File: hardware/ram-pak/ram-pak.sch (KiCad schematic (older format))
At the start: 16 parts, among them J1 PinHeader_2x22_P1.27mm, U1 TLV62568DBV

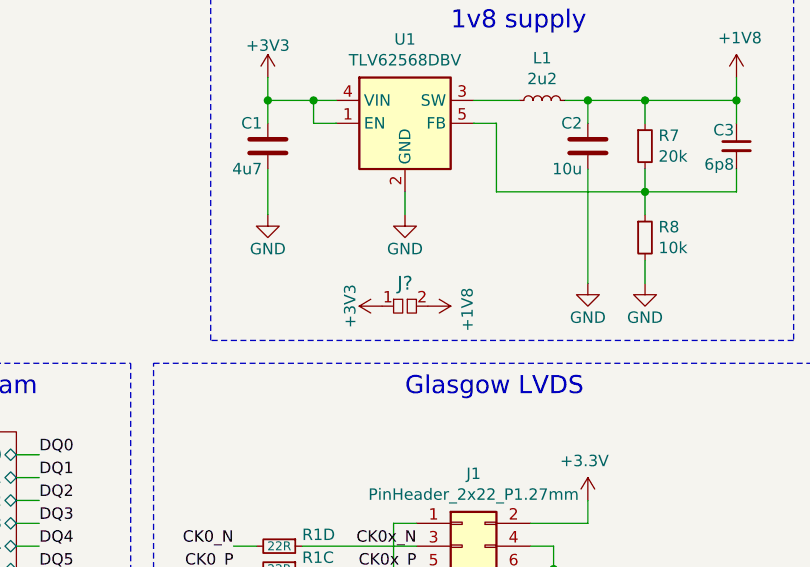
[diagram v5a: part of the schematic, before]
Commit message: ram-pak: Increased pad hole gap for improved assembly.
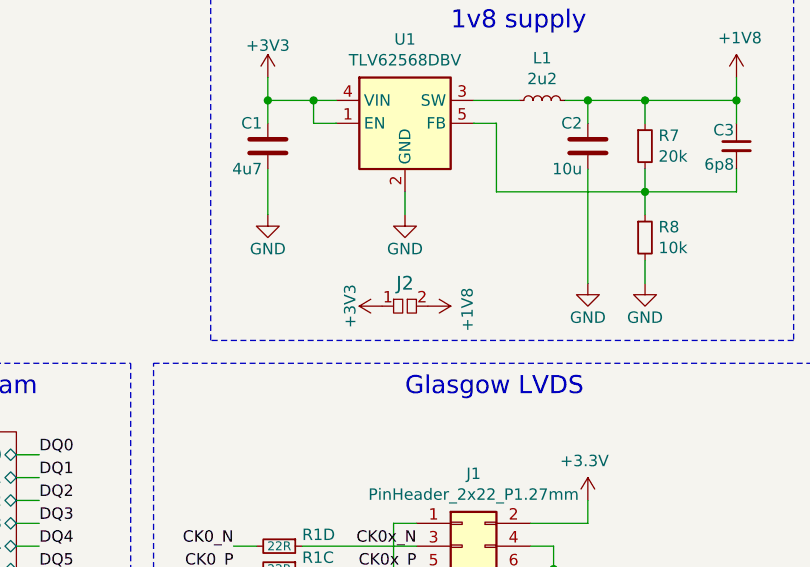
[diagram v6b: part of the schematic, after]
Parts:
- gave numbers to parts that had none: 1
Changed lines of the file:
@@
 DQ5x
 $Comp
-L pkl_misc:pkl_jumper J?
+L pkl_misc:pkl_jumper J2
 U 1 1 602E83F4
 P 6050 2500
-F 0 "J?" H 6050 2600 60  0000 C CNN
+F 0 "J2" H 6050 2600 60  0000 C CNN
 F 1 "pkl_jumper" H 6050 2641 60  0001 C CNN
 F 2 "pkl_jumpers:J_0603" H 6050 2500 60  0001 C CNN
@@
 $EndComp
 $Comp
-L power:+3V3 #PWR?
+L power:+3V3 #PWR0107
 U 1 1 602E9589
 P 5950 2500
-F 0 "#PWR?" H 5950 2350 50  0001 C CNN
+F 0 "#PWR0107" H 5950 2350 50  0001 C CNN
 F 1 "+3V3" H 5950 2640 50  0000 C CNN
 F 2 "" H 5950 2500 60  0000 C CNN
@@
 $EndComp
 $Comp
-L power:+1V8 #PWR?
+L power:+1V8 #PWR0108
 U 1 1 602EA3A9
 P 6150 2500
-F 0 "#PWR?" H 6150 2350 50  0001 C CNN
+F 0 "#PWR0108" H 6150 2350 50  0001 C CNN
 F 1 "+1V8" H 6165 2673 50  0000 C CNN
 F 2 "" H 6150 2500 50  0001 C CNN
